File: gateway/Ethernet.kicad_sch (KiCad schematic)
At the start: 9 parts, among them X1301 Ethernet

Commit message: Working on version 1.0
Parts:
- C1301, C1302: footprint Capacitor_SMD:C_0402_1005Metric -> Capacitor_SMD:C_0805_2012Metric; manf# 04025C104JAT2A -> 08053C104M4T4A; mouser# 581-04025C104JAT2A -> 581-08053C104M4T4A
- R1301, R1302: manf# CR0402-JW-471GLF -> CR0805-JW-471GLF; mouser# 652-CR0402-JW-471GLF -> 652-CR0805-JW-471GLF
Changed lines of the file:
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@@
 			)
 		)
-		(property "Footprint" "Capacitor_SMD:C_0402_1005Metric"
+		(property "Footprint" "Capacitor_SMD:C_0805_2012Metric"
 			(at 184.4548 181.61 0)
 			(hide yes)
@@
 			)
 		)
-		(property "Datasheet" "https://datasheets.kyocera-avx.com/KGM_X7R.pdf"
+		(property "Datasheet" "https://datasheets.kyocera-avx.com/AutoMLCC.pdf"
 			(at 185.42 177.8 0)
 			(hide yes)
@@
 			)
 		)
-		(property "manf#" "04025C104JAT2A"
+		(property "manf#" "08053C104M4T4A"
 			(at 185.42 177.8 0)
 			(hide yes)
@@
 			)
 		)
-		(property "mouser#" "581-04025C104JAT2A"
+		(property "mouser#" "581-08053C104M4T4A"
 			(at 185.42 177.8 0)
 			(hide yes)
@@
 			)
 		)
-		(property "Footprint" "Capacitor_SMD:C_0402_1005Metric"
+		(property "Footprint" "Capacitor_SMD:C_0805_2012Metric"
 			(at 191.4652 181.61 0)
 			(hide yes)
@@
 			)
 		)
-		(property "Datasheet" "https://datasheets.kyocera-avx.com/KGM_X7R.pdf"
+		(property "Datasheet" "https://datasheets.kyocera-avx.com/AutoMLCC.pdf"
 			(at 190.5 177.8 0)
 			(hide yes)
@@
 			)
 		)
-		(property "manf#" "04025C104JAT2A"
+		(property "manf#" "08053C104M4T4A"
 			(at 190.5 177.8 0)
 			(hide yes)
@@
 			)
 		)
-		(property "mouser#" "581-04025C104JAT2A"
+		(property "mouser#" "581-08053C104M4T4A"
 			(at 190.5 177.8 0)
 			(hide yes)
@@
 			)
 		)
-		(property "manf#" "CR0402-JW-471GLF"
+		(property "manf#" "CR0805-JW-471GLF"
 			(at 207.01 181.61 0)
 			(hide yes)
@@
 			)
 		)
-		(property "mouser#" "652-CR0402-JW-471GLF"
+		(property "mouser#" "652-CR0805-JW-471GLF"
 			(at 207.01 181.61 0)
 			(hide yes)
@@
 			)
 		)
-		(property "manf#" "CR0402-JW-471GLF"
+		(property "manf#" "CR0805-JW-471GLF"
 			(at 217.17 107.95 0)
 			(hide yes)
@@
 			)
 		)
-		(property "mouser#" "652-CR0402-JW-471GLF"
+		(property "mouser#" "652-CR0805-JW-471GLF"
 			(at 217.17 107.95 0)
 			(hide yes)

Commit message: Working on PCB
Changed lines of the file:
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@@
+	)
+	(junction
+		(at 269.24 179.07)
+		(diameter 0)
+		(color 0 0 0 0)
 	)
 	(junction
@@
 		)
 	)
-	(bus
-		(pts
-			(xy 179.07 106.68) (xy 179.07 111.76)
-		)
-		(stroke
-			(width 0)
-			(type default)
-		)
-	)
 	(wire
 		(pts
@@
 	(wire
 		(pts
+			(xy 269.24 177.8) (xy 269.24 179.07)
+		)
+		(stroke
+			(width 0)
+			(type default)
+		)
+	)
+	(wire
+		(pts
 			(xy 185.42 134.62) (xy 185.42 173.99)
 		)
@@
 	(bus
 		(pts
-			(xy 177.8 106.68) (xy 179.07 106.68)
+			(xy 177.8 111.76) (xy 179.07 111.76)
 		)
 		(stroke
@@
 	(hierarchical_label "Ethernet{Ethernet}"
 		(shape bidirectional)
-		(at 177.8 106.68 180)
+		(at 177.8 111.76 180)
 		(effects
 			(font
@@
 					(unit 1)
 				)
+			)
+		)
+	)
+	(symbol
+		(lib_id "power:PWR_FLAG")
+		(at 269.24 177.8 0)
+		(unit 1)
+		(body_style 1)
+		(exclude_from_sim no)
+		(in_bom yes)
+		(on_board yes)
+		(in_pos_files yes)
+		(dnp no)
+		(fields_autoplaced yes)
+		(property "Reference" "#FLG01301"
+			(at 269.24 175.895 0)
+			(hide yes)
+			(show_name no)
+			(do_not_autoplace no)
+			(effects
+				(font
+					(size 1.27 1.27)
+				)
+			)
+		)
+		(property "Value" "PWR_FLAG"
+			(at 269.24 172.72 0)
+			(show_name no)
+			(do_not_autoplace no)
+			(effects
+				(font
+					(size 1.27 1.27)
+				)
+			)
+		)
+		(property "Footprint" ""
+			(at 269.24 177.8 0)
+			(hide yes)
+			(show_name no)
+			(do_not_autoplace no)
+			(effects
+				(font
+					(size 1.27 1.27)
+				)
+			)
+		)
+		(property "Datasheet" ""
+			(at 269.24 177.8 0)
+			(hide yes)
+			(show_name no)
+			(do_not_autoplace no)
+			(effects
+				(font
+					(size 1.27 1.27)
+				)
+			)
+		)
+		(property "Description" "Special symbol for telling ERC where power comes from"
+			(at 269.24 177.8 0)
+			(hide yes)
+			(show_name no)
+			(do_not_autoplace no)
+			(effects
+				(font
+					(size 1.27 1.27)
+				)
+			)
+		)
+		(pin "1"
+		)
+		(instances
+			(project "Gateway"
+				(path "/d5742f03-3b1a-42e5-a384-018bd4b919aa/c5103ceb-5325-4a84-a025-9638a412984e/86891732-a753-4dcc-a58c-71e3fc99b0cd"
+					(reference "#FLG01301")
+					(unit 1)
+				)

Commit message: Adding level shifter, update documentation
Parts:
- TP1301, TP1302: value (none) -> ~
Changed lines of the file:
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@@
 			)
 		)
-		(property "Value" ""
+		(property "Value" "~"
 			(at 227.33 93.345 0)
 			(show_name no)
@@
 			)
 		)
-		(property "Value" ""
+		(property "Value" "~"
 			(at 227.33 76.835 0)
 			(show_name no)

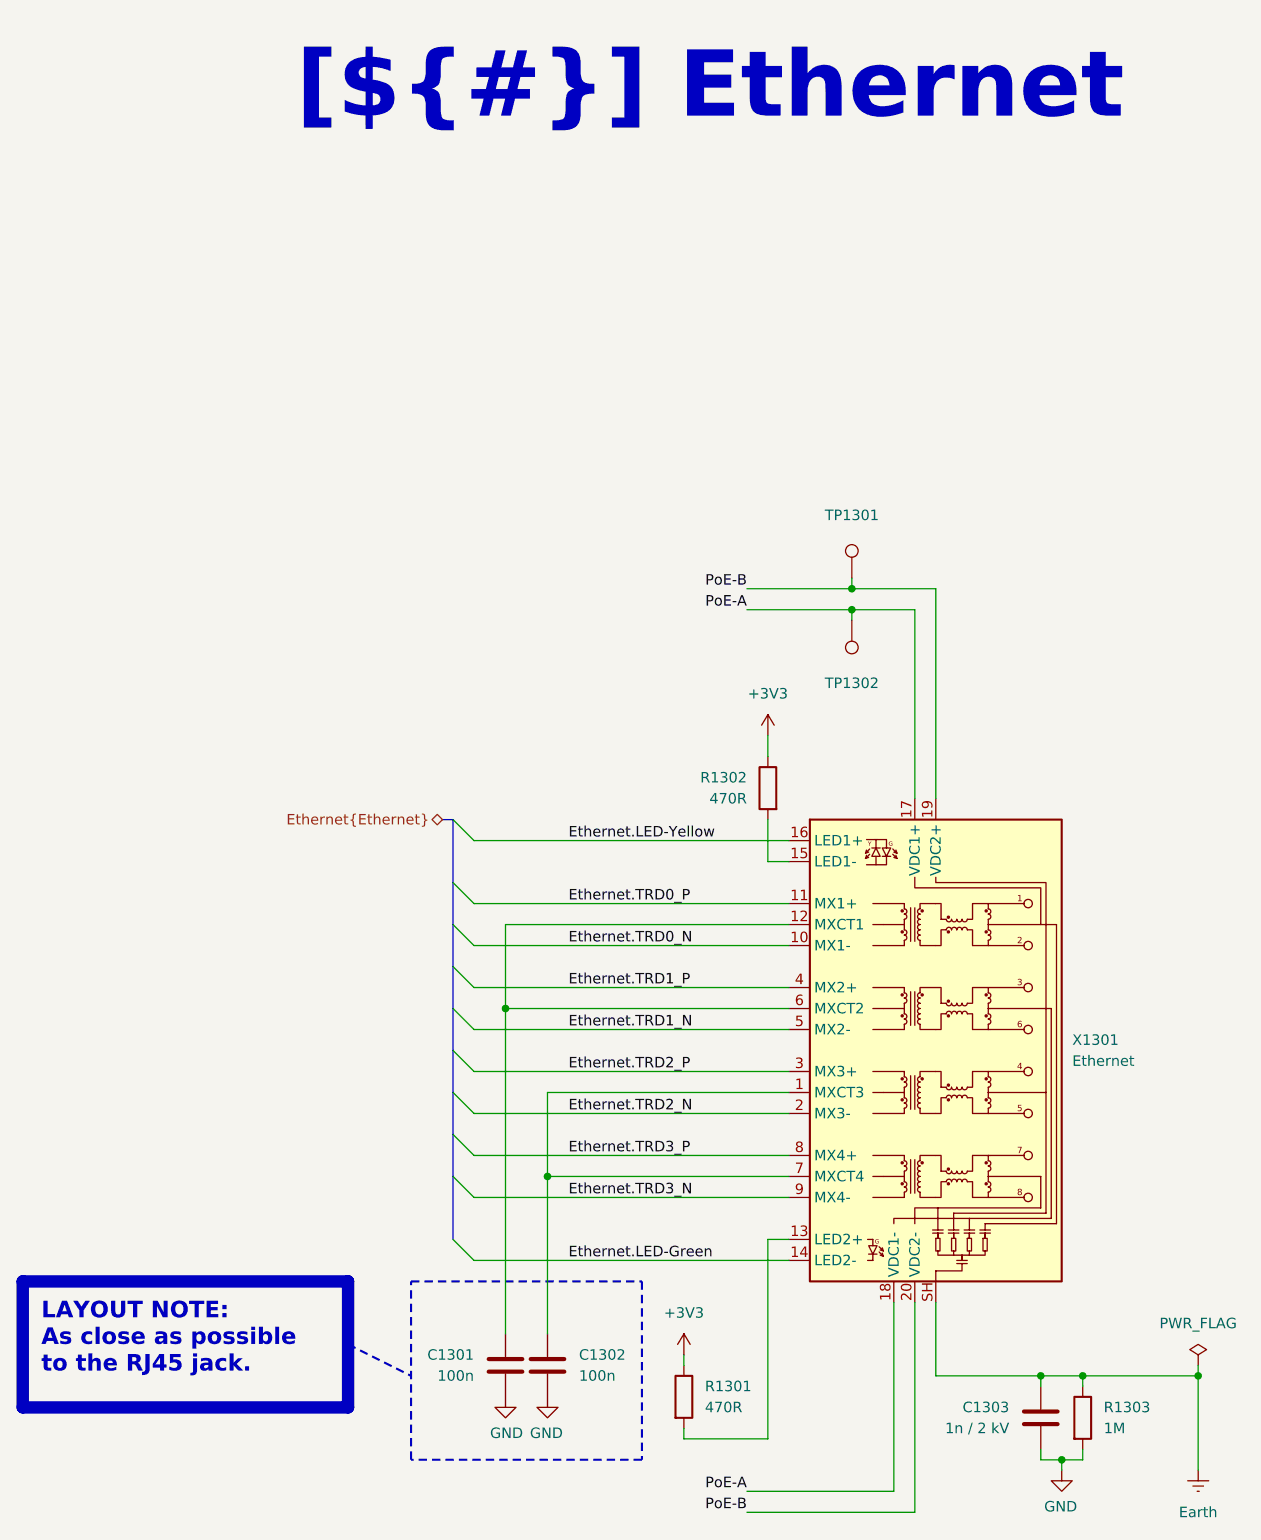
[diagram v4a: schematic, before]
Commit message: Replace level shifter, replace CC2530 with CC2652, fix wrong part numbers
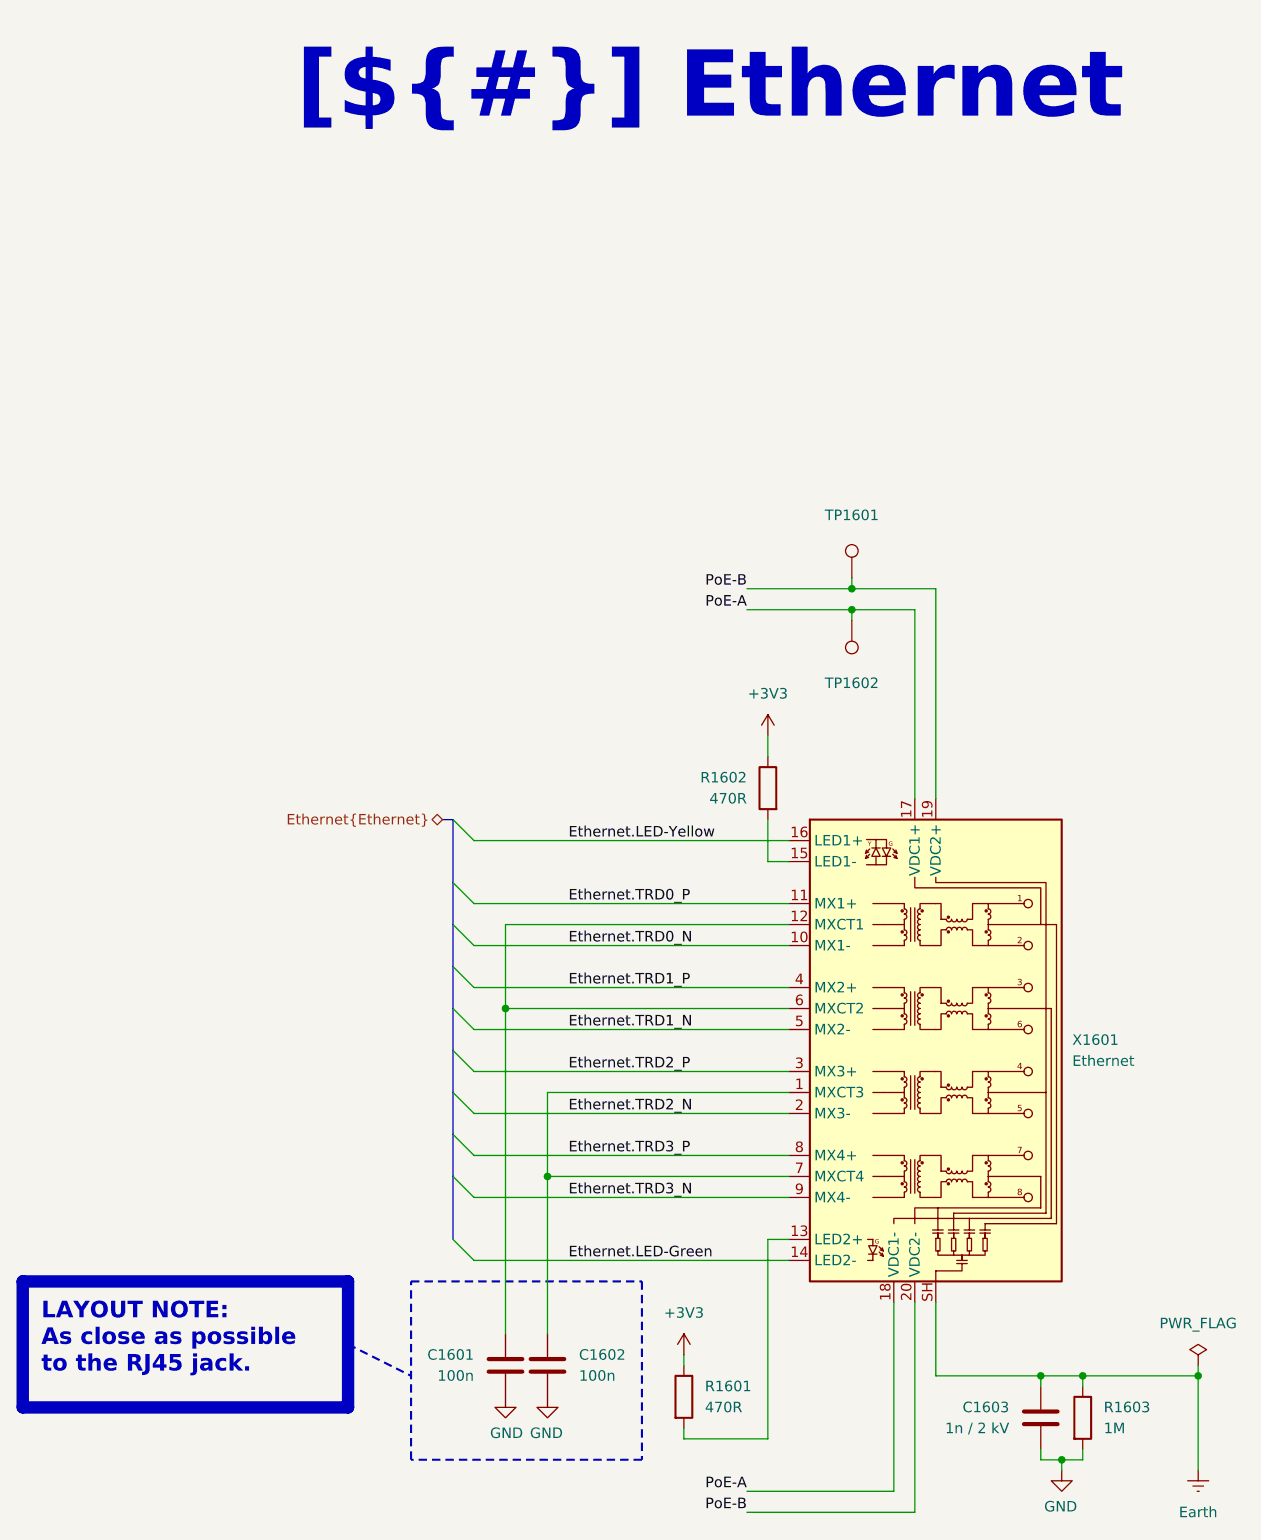
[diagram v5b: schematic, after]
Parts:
- R1601: renamed from R1301; footprint Resistor_SMD:R_0402_1005Metric -> Resistor_SMD:R_0805_2012Metric
- R1602: renamed from R1302; footprint Resistor_SMD:R_0402_1005Metric -> Resistor_SMD:R_0805_2012Metric
- renumbered C1301 to C1601, C1302 to C1602, C1303 to C1603, R1303 to R1603, TP1301 to TP1601, TP1302 to TP1602, X1301 to X1601
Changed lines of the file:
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@@
 		(in_pos_files yes)
 		(dnp no)
-		(property "Reference" "R1303"
+		(property "Reference" "R1603"
 			(at 257.81 182.8799 0)
 			(show_name no)
@@
 			(project "Gateway"
 				(path "/d5742f03-3b1a-42e5-a384-018bd4b919aa/c5103ceb-5325-4a84-a025-9638a412984e/86891732-a753-4dcc-a58c-71e3fc99b0cd"
-					(reference "R1303")
+					(reference "R1603")
 					(unit 1)
 				)
@@
 		(in_pos_files no)
 		(dnp no)
-		(property "Reference" "TP1302"
+		(property "Reference" "TP1602"
 			(at 227.33 95.25 0)
 			(show_name no)
@@
 			(project "Gateway"
 				(path "/d5742f03-3b1a-42e5-a384-018bd4b919aa/c5103ceb-5325-4a84-a025-9638a412984e/86891732-a753-4dcc-a58c-71e3fc99b0cd"
-					(reference "TP1302")
+					(reference "TP1602")
 					(unit 1)
 				)
@@
 		(in_pos_files yes)
 		(dnp no)
-		(property "Reference" "C1303"
+		(property "Reference" "C1603"
 			(at 246.38 182.8799 0)
 			(show_name no)
@@
 			(project "Gateway"
 				(path "/d5742f03-3b1a-42e5-a384-018bd4b919aa/c5103ceb-5325-4a84-a025-9638a412984e/86891732-a753-4dcc-a58c-71e3fc99b0cd"
-					(reference "C1303")
+					(reference "C1603")
 					(unit 1)
 				)
@@
 		(in_pos_files yes)
 		(dnp no)
-		(property "Reference" "#PWR01301"
+		(property "Reference" "#PWR01601"
 			(at 185.42 187.96 0)
 			(hide yes)
@@
 			(project "Gateway"
 				(path "/d5742f03-3b1a-42e5-a384-018bd4b919aa/c5103ceb-5325-4a84-a025-9638a412984e/86891732-a753-4dcc-a58c-71e3fc99b0cd"
-					(reference "#PWR01301")
+					(reference "#PWR01601")
 					(unit 1)
 				)
@@
 		(dnp no)
 		(fields_autoplaced yes)
-		(property "Reference" "#PWR01306"
+		(property "Reference" "#PWR01606"
 			(at 269.24 196.85 0)
 			(hide yes)
@@
 			(project "Gateway"
 				(path "/d5742f03-3b1a-42e5-a384-018bd4b919aa/c5103ceb-5325-4a84-a025-9638a412984e/86891732-a753-4dcc-a58c-71e3fc99b0cd"
-					(reference "#PWR01306")
+					(reference "#PWR01606")
 					(unit 1)
 				)
@@
 		(dnp no)
 		(fields_autoplaced yes)
-		(property "Reference" "#FLG01301"
+		(property "Reference" "#FLG01601"
 			(at 269.24 175.895 0)
 			(hide yes)
@@
 			(project "Gateway"
 				(path "/d5742f03-3b1a-42e5-a384-018bd4b919aa/c5103ceb-5325-4a84-a025-9638a412984e/86891732-a753-4dcc-a58c-71e3fc99b0cd"
-					(reference "#FLG01301")
+					(reference "#FLG01601")
 					(unit 1)
 				)
@@
 		(in_pos_files yes)
 		(dnp no)
-		(property "Reference" "C1301"
+		(property "Reference" "C1601"
 			(at 181.61 176.5299 0)
 			(show_name no)
@@
 			(project "Gateway"
 				(path "/d5742f03-3b1a-42e5-a384-018bd4b919aa/c5103ceb-5325-4a84-a025-9638a412984e/86891732-a753-4dcc-a58c-71e3fc99b0cd"
-					(reference "C1301")
+					(reference "C1601")
 					(unit 1)
 				)
@@
 		(dnp no)
 		(fields_autoplaced yes)
-		(property "Reference" "#PWR01303"
+		(property "Reference" "#PWR01603"
 			(at 207.01 180.34 0)
 			(hide yes)
@@
 			(project "Gateway"
 				(path "/d5742f03-3b1a-42e5-a384-018bd4b919aa/c5103ceb-5325-4a84-a025-9638a412984e/86891732-a753-4dcc-a58c-71e3fc99b0cd"
-					(reference "#PWR01303")
+					(reference "#PWR01603")
 					(unit 1)
 				)
@@
 		(in_pos_files no)
 		(dnp no)
-		(property "Reference" "TP1301"
+		(property "Reference" "TP1601"
 			(at 227.33 74.93 0)
 			(show_name no)
@@
 			(project "Gateway"
 				(path "/d5742f03-3b1a-42e5-a384-018bd4b919aa/c5103ceb-5325-4a84-a025-9638a412984e/86891732-a753-4dcc-a58c-71e3fc99b0cd"
-					(reference "TP1301")
+					(reference "TP1601")
 					(unit 1)
 				)
@@
 		(dnp no)
 		(fields_autoplaced yes)
-		(property "Reference" "#PWR01304"
+		(property "Reference" "#PWR01604"
 			(at 217.17 105.41 0)
 			(hide yes)
@@
 			(project "Gateway"
 				(path "/d5742f03-3b1a-42e5-a384-018bd4b919aa/c5103ceb-5325-4a84-a025-9638a412984e/86891732-a753-4dcc-a58c-71e3fc99b0cd"
-					(reference "#PWR01304")
+					(reference "#PWR01604")
 					(unit 1)
 				)
@@
 		(in_pos_files yes)
 		(dnp no)
-		(property "Reference" "C1302"
+		(property "Reference" "C1602"
 			(at 194.31 176.5299 0)
 			(show_name no)
@@
 			(project "Gateway"
 				(path "/d5742f03-3b1a-42e5-a384-018bd4b919aa/c5103ceb-5325-4a84-a025-9638a412984e/86891732-a753-4dcc-a58c-71e3fc99b0cd"
-					(reference "C1302")
+					(reference "C1602")
 					(unit 1)
 				)
@@
 		(in_pos_files yes)
 		(dnp no)
-		(property "Reference" "R1301"
+		(property "Reference" "R1601"
 			(at 209.55 180.3399 0)
 			(show_name no)
@@
 			)
 		)
-		(property "Footprint" "Resistor_SMD:R_0402_1005Metric"
+		(property "Footprint" "Resistor_SMD:R_0805_2012Metric"
 			(at 205.232 181.61 90)
 			(hide yes)
@@
 			(project "Gateway"
 				(path "/d5742f03-3b1a-42e5-a384-018bd4b919aa/c5103ceb-5325-4a84-a025-9638a412984e/86891732-a753-4dcc-a58c-71e3fc99b0cd"
-					(reference "R1301")
+					(reference "R1601")
 					(unit 1)
 				)
@@
 		(in_pos_files yes)
 		(dnp no)
-		(property "Reference" "R1302"
+		(property "Reference" "R1602"
 			(at 214.63 106.6799 0)
 			(show_name no)
@@
 			)
 		)
-		(property "Footprint" "Resistor_SMD:R_0402_1005Metric"
+		(property "Footprint" "Resistor_SMD:R_0805_2012Metric"
 			(at 218.948 107.95 90)
 			(hide yes)
@@
 			(project "Gateway"
 				(path "/d5742f03-3b1a-42e5-a384-018bd4b919aa/c5103ceb-5325-4a84-a025-9638a412984e/86891732-a753-4dcc-a58c-71e3fc99b0cd"
-					(reference "R1302")
+					(reference "R1602")
 					(unit 1)
 				)
@@
 		(in_pos_files yes)
 		(dnp no)
-		(property "Reference" "#PWR01305"
+		(property "Reference" "#PWR01605"
 			(at 252.73 196.85 0)
 			(hide yes)
@@
 			(project "Gateway"
 				(path "/d5742f03-3b1a-42e5-a384-018bd4b919aa/c5103ceb-5325-4a84-a025-9638a412984e/86891732-a753-4dcc-a58c-71e3fc99b0cd"
-					(reference "#PWR01305")
+					(reference "#PWR01605")
 					(unit 1)
 				)
@@
 		(in_pos_files yes)
 		(dnp no)
-		(property "Reference" "#PWR01302"
+		(property "Reference" "#PWR01602"
 			(at 190.5 187.96 0)
 			(hide yes)
@@
 			(project "Gateway"
 				(path "/d5742f03-3b1a-42e5-a384-018bd4b919aa/c5103ceb-5325-4a84-a025-9638a412984e/86891732-a753-4dcc-a58c-71e3fc99b0cd"
-					(reference "#PWR01302")
+					(reference "#PWR01602")
 					(unit 1)
 				)
@@
 		(dnp no)
 		(fields_autoplaced yes)
-		(property "Reference" "X1301"
+		(property "Reference" "X1601"
 			(at 254 138.4299 0)
 			(show_name no)
@@
 			(project "Gateway"
 				(path "/d5742f03-3b1a-42e5-a384-018bd4b919aa/c5103ceb-5325-4a84-a025-9638a412984e/86891732-a753-4dcc-a58c-71e3fc99b0cd"
-					(reference "X1301")
+					(reference "X1601")
 					(unit 1)
 				)
